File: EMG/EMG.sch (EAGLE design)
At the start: 57 parts, among them IC1 TL074CD, IC2 TL074CD, IC3 TL074CD, J1 SJ-3523-SMT-TR, J3 640455-5

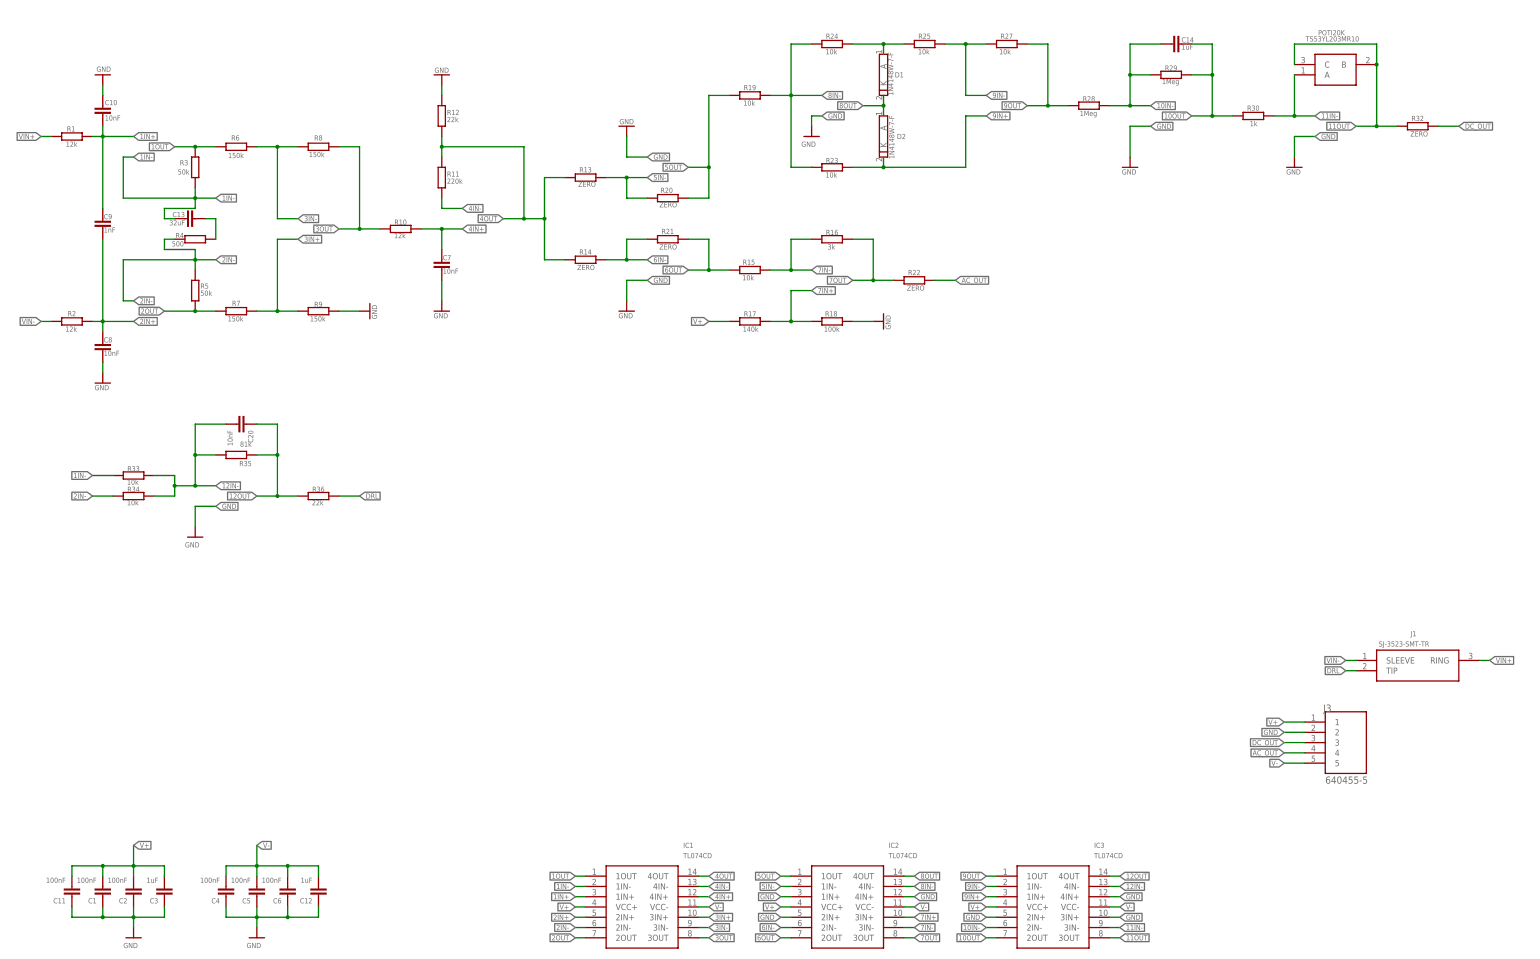
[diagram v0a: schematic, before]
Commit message: Added pictures for EMG and Mainboard for final report
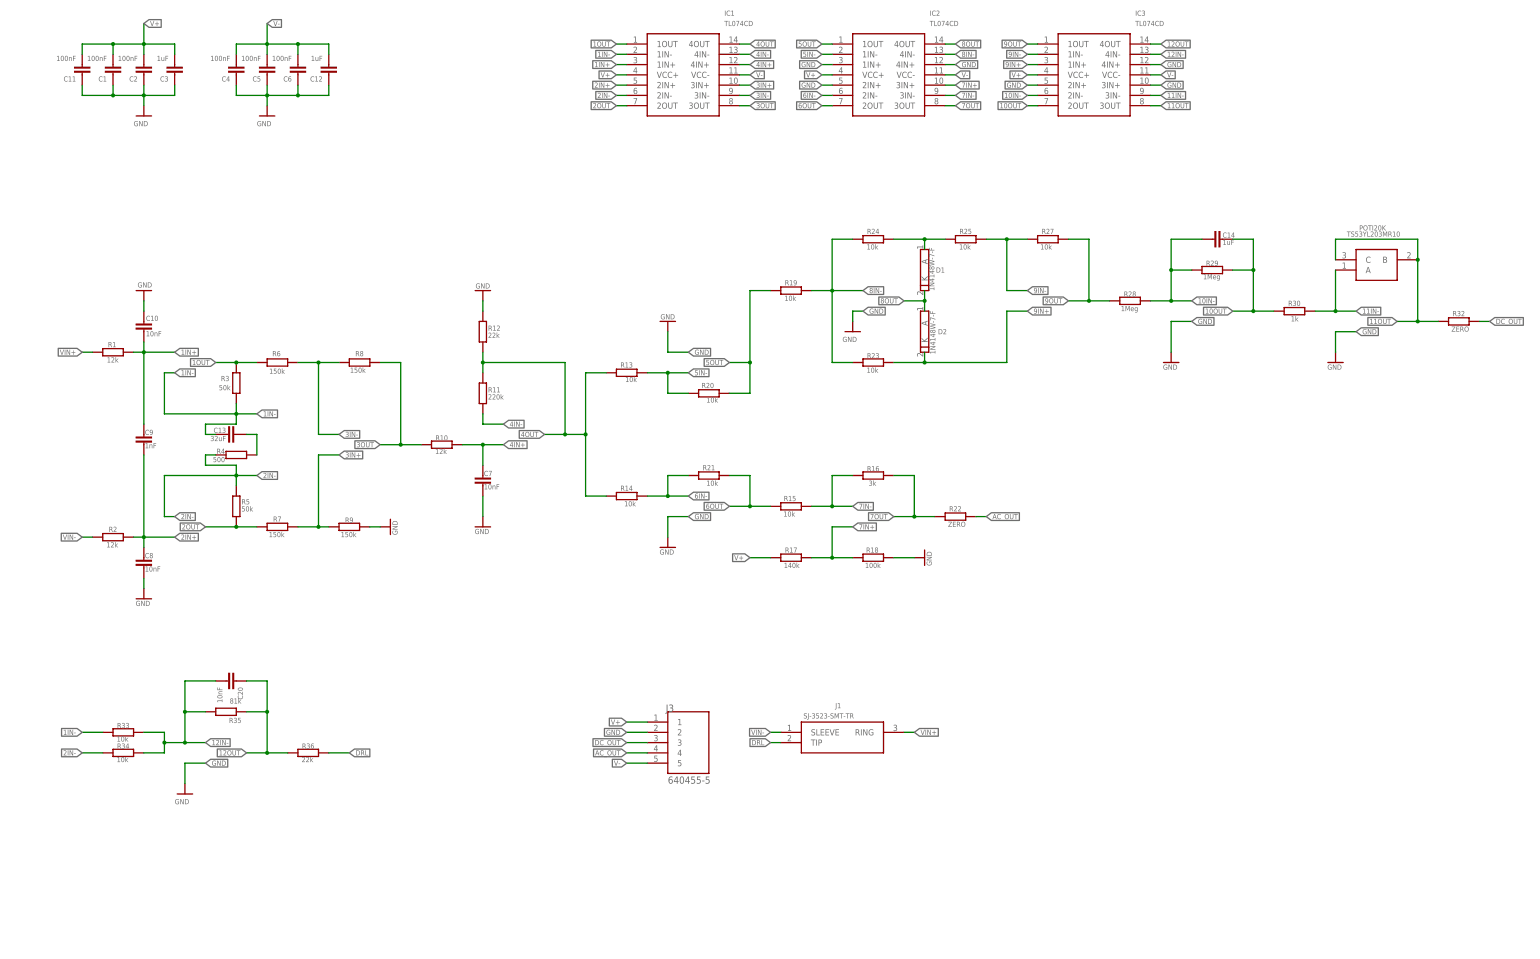
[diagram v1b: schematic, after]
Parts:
- R13, R14, R20, R21: value ZERO -> 10k
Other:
- note added: "Connector for electrodes"
- note added: "Connector to Mainboard"
- note added: "Driven Right Leg Circuit"
- note added: "Instrumentational Amplifier"
- note added: "Integrator"
- note added: "Inverting Amplifier"
- note added: "Lowpass-Filter & Non-Inverting Amplifier"
- note added: "Operational Amplifiers Overview"
- note added: "Power Supply Buffering"
- note added: "Precision Rectifier"
- note added: "Two Inverting Amplifier Stages and Offset-Addition for having a positive alternating signal in Microcontroller input range"
- moved on the sheet: C1, C10, C11, C12, C13, C14, C2, C20, C3, C4, C5, C6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
